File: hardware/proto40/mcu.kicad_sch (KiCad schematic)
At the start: 20 parts, among them J201 Conn_ARM_SWD_TagConnect_TC2030, J202 UART, SW201 START, U201 STM32C071C8Tx

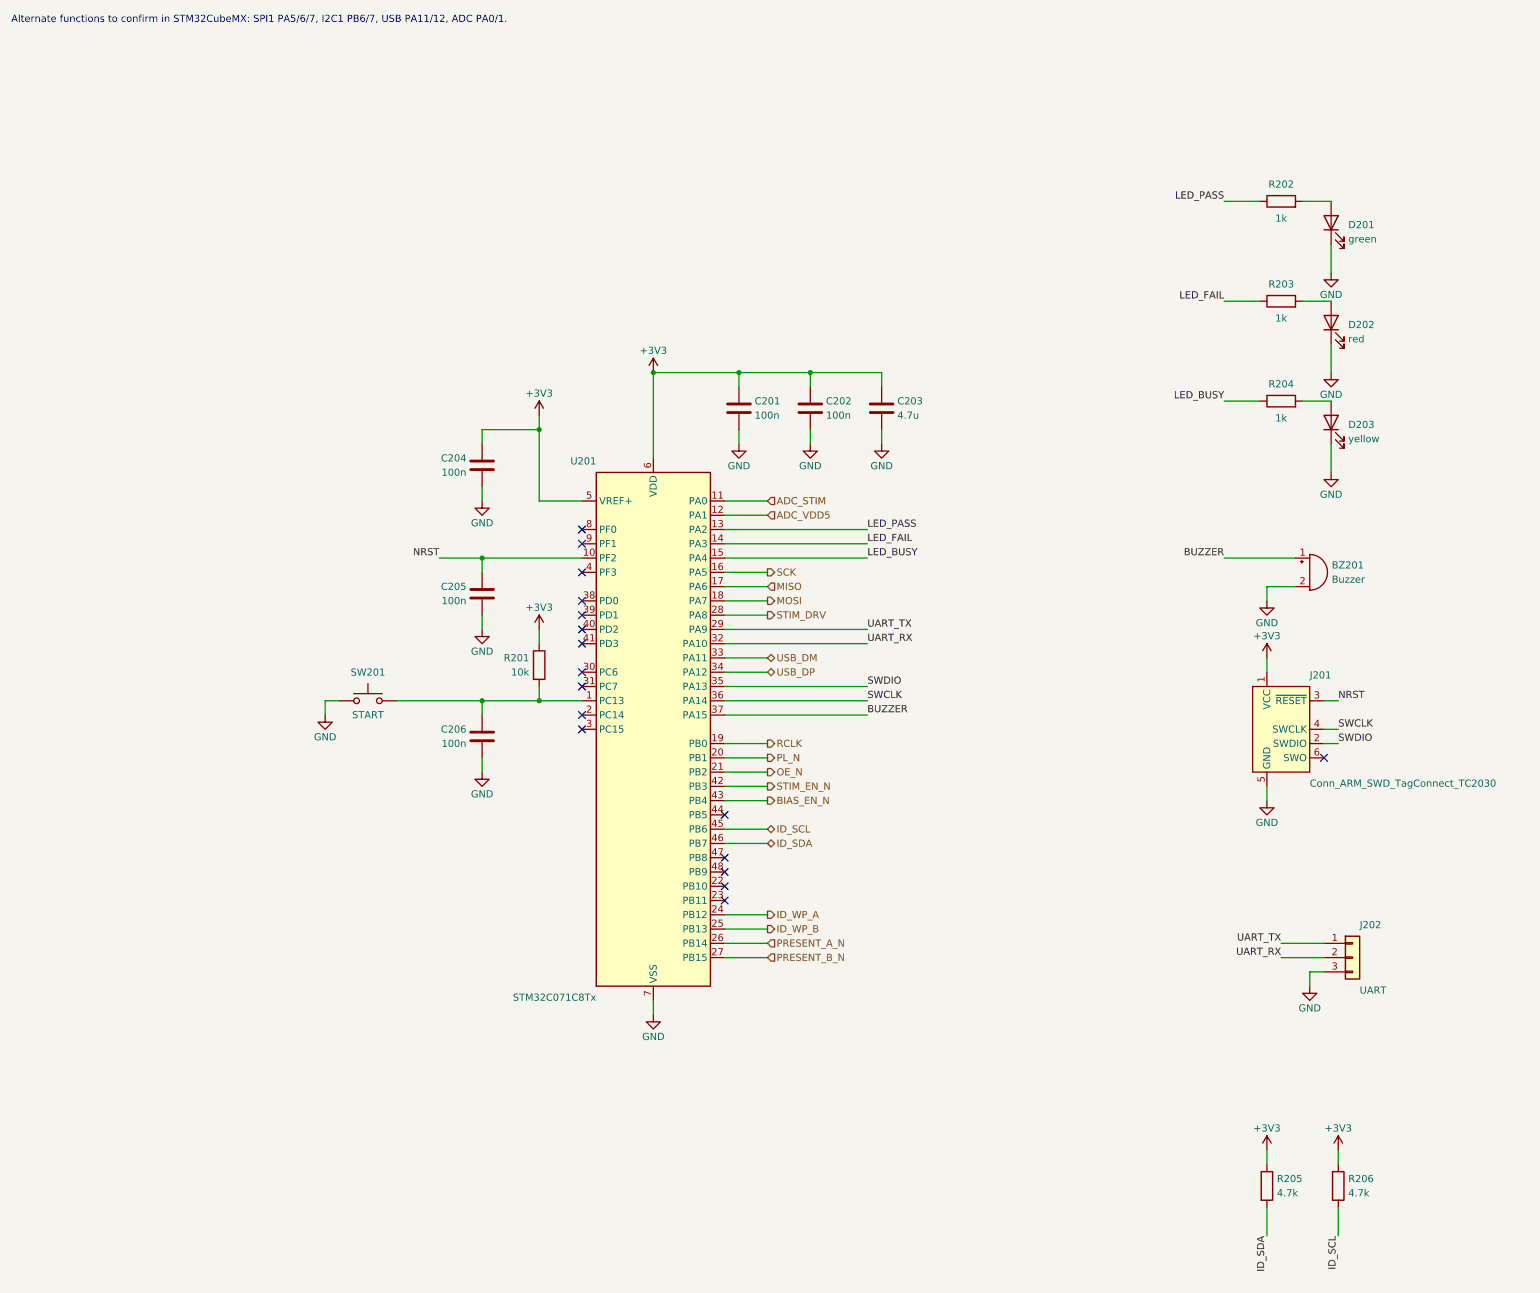
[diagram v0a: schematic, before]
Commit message: Resolve Proto40 house-style review findings
- Fixture ID lines: TVS at the connector plus series R on SDA/SCL/WP/A0/PRESENT_N;
  ID_VCC limited by 100 ohm 1206 (D14). PRESENT_N pull-up moved to MCU side.
- Shunt clamp ballast R104 is 6.8 ohm 2512, BCP53 copper note (D15).
- MPN/Manufacturer on every part (generic Yageo/Samsung passives), LCSC TBD.
- Test points on the '595 outputs and chain in/out; pull-downs on SCK/RCLK.
- Root sheet: CTRL/SENSE chains and ID lines drawn as wires; ASCII-only text.
- layoutcheck: non-ASCII, title length, text/text gap, text/wire clearance,
  NC flag on wired pin; wider char estimate. CI ERC runs --severity-all.
- Netclass patterns tightened for STIM/MUX and SPI nets.

Co-Authored-By: Claude Opus 5.5 (1M context) <noreply@anthropic.com>
Claude-Session: https://claude.ai/code/session_013SDanWEFU4wFXEYfZ6C9GH
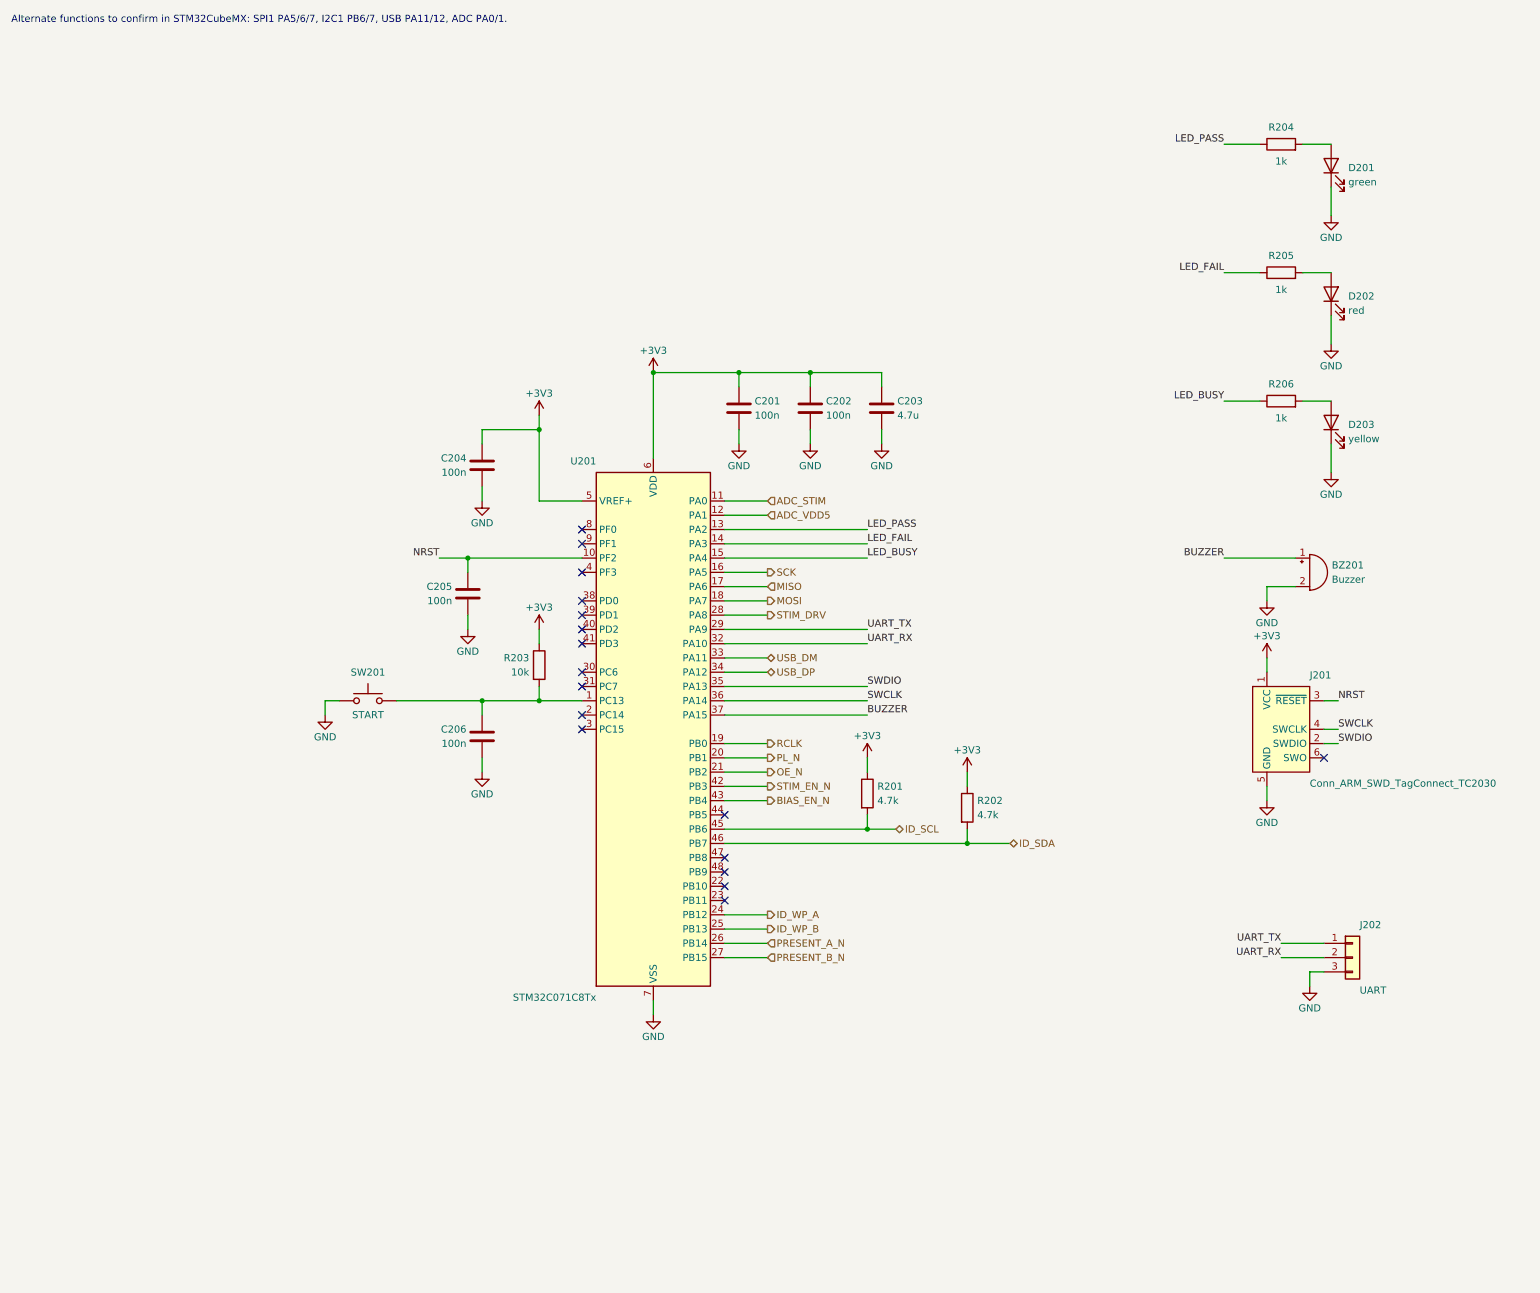
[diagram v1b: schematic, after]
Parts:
- BZ201: LCSC (none) -> TBD; MPN (none) -> TBD: passive piezo, 12 x 9.5 mm, 7.6 mm pitch; Note passive piezo, GPIO PWM -> GPIO PWM
- C201, C202, C204, C205, C206: LCSC (none) -> TBD; MPN (none) -> CL10B104KB8NNNC; Manufacturer (none) -> Samsung Electro-Mechanics
- C203: LCSC (none) -> TBD; MPN (none) -> CL21A475KAQNNNE; Manufacturer (none) -> Samsung Electro-Mechanics
- D201: LCSC (none) -> TBD; MPN (none) -> KT-0603G; Manufacturer (none) -> Hubei KENTO Elec
- D202: LCSC (none) -> TBD; MPN (none) -> KT-0603R; Manufacturer (none) -> Hubei KENTO Elec
- D203: LCSC (none) -> TBD; MPN (none) -> KT-0603Y; Manufacturer (none) -> Hubei KENTO Elec
- J201: LCSC (none) -> none; MPN (none) -> none (Tag-Connect pads, cable TC2030-IDC-NL)
- J202: LCSC (none) -> TBD; MPN (none) -> TBD: 1x03 2.54 mm pin header
- R201: value 10k -> 4.7k; LCSC (none) -> TBD; MPN (none) -> RC0603FR-074K7L; Manufacturer (none) -> Yageo
- R202: value 1k -> 4.7k; LCSC (none) -> TBD; MPN (none) -> RC0603FR-074K7L; Manufacturer (none) -> Yageo
- R203: value 1k -> 10k; LCSC (none) -> TBD; MPN (none) -> RC0603FR-0710KL; Manufacturer (none) -> Yageo
- R204: LCSC (none) -> TBD; MPN (none) -> RC0603FR-071KL; Manufacturer (none) -> Yageo
- R205, R206: value 4.7k -> 1k; LCSC (none) -> TBD; MPN (none) -> RC0603FR-071KL; Manufacturer (none) -> Yageo
- SW201: LCSC (none) -> TBD; MPN (none) -> TL3342F160QG; Manufacturer (none) -> E-Switch
- U201: LCSC (none) -> TBD
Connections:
- net +3V3: now also R202.1, R203.1; no longer R205.1, R206.1
- net ID_SCL: now also R201.2; no longer R206.2
- net ID_SDA: now also R202.2; no longer R205.2
- net LED_BUSY: now also R206.1; no longer R204.1
- net LED_FAIL: now also R205.1; no longer R203.1
- net LED_PASS: now also R204.1; no longer R202.1
- net at R204.2: now also D201.2 (A); no longer D203.2 (A)
- net at C206.1, SW201.2, U201.1 (PC13): now also R203.2; no longer R201.2
- net at D202.2 (A): now also R205.2; no longer R203.2
- new net: D203.2 (A), R206.2
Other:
- title: Proto40 – STM32C071 controller, UI, debug -> Proto40 - STM32C071 controller, UI, debug
- moved on the sheet: C205, D201, D202, R201, R202, R203, R204, R205, R206
